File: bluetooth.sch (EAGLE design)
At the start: 28 parts, among them U1 NRF8001, X1 16MHz, X2 32.768kHz

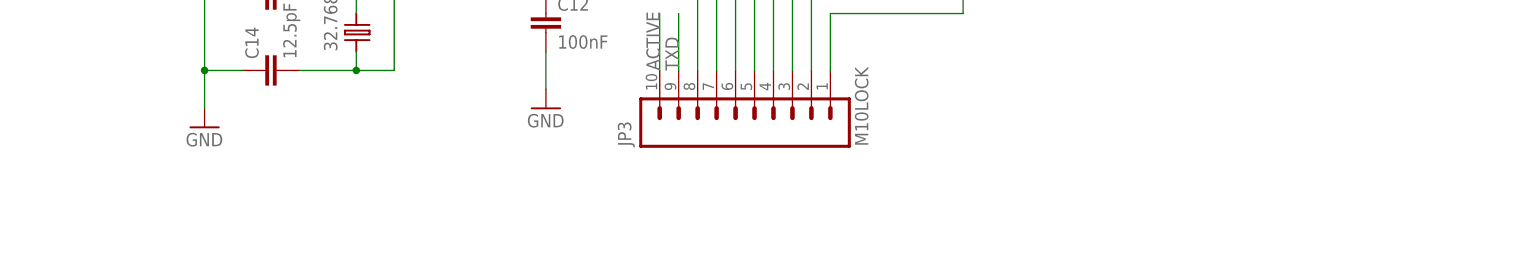
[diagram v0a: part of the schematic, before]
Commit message: fix readme
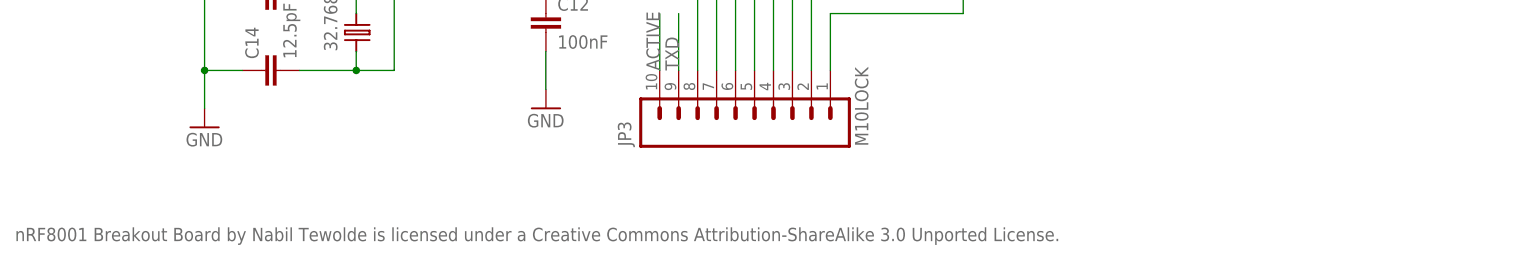
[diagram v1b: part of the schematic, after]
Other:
- note added: "nRF8001 Breakout Board by Nabil Tewolde is licensed under a Creative Commons Attribution-ShareAlike 3.0 Unported License."
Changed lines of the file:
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@@
 <sheet>
 <plain>
+<text x="-15.24" y="-22.86" size="1.778" layer="95">nRF8001 Breakout Board by Nabil Tewolde is licensed under a Creative Commons Attribution-ShareAlike 3.0 Unported License.</text>
 </plain>
 <instances>

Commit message: Connected pin 9 (power) to VDD. Oops
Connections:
- removed net N$8: C12.1, U1.VDD@2
- net VDD: now also C12.1, U1.VDD@2
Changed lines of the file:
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@@
-</segment>
-</net>
-<net name="N$8" class="0">
-<segment>
-<pinref part="U1" gate="G$1" pin="VDD@2"/>
-<wire x1="73.66" y1="17.78" x2="73.66" y2="10.16" width="0.1524" layer="91"/>
-<pinref part="C12" gate="G$1" pin="1"/>
-<wire x1="73.66" y1="10.16" x2="55.88" y2="10.16" width="0.1524" layer="91"/>
 </segment>
 </net>
@@
 <label x="25.4" y="116.84" size="1.778" layer="95"/>
 </segment>
-</net>
+<segment>
+<pinref part="U1" gate="G$1" pin="VDD@2"/>
+<wire x1="73.66" y1="17.78" x2="73.66" y2="10.16" width="0.1524" layer="91"/>
+<pinref part="C12" gate="G$1" pin="1"/>
+<wire x1="73.66" y1="10.16" x2="55.88" y2="10.16" width="0.1524" layer="91"/>
+</segment>
+</net>
